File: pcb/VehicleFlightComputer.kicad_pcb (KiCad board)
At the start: 4 copper layers, 50 x 50 mm, 54 parts, among them J1 FFC2B28-24-G, J3 USB_C_Receptacle, J4 Debug, Q1 S8050, SW1 B3U-1000P, U1 STM32H533VET6, U2 LIS2MDL, U3 LSM6DSV32X, U4 MCP2221A-I/ST, U5 AP2112K-3.3

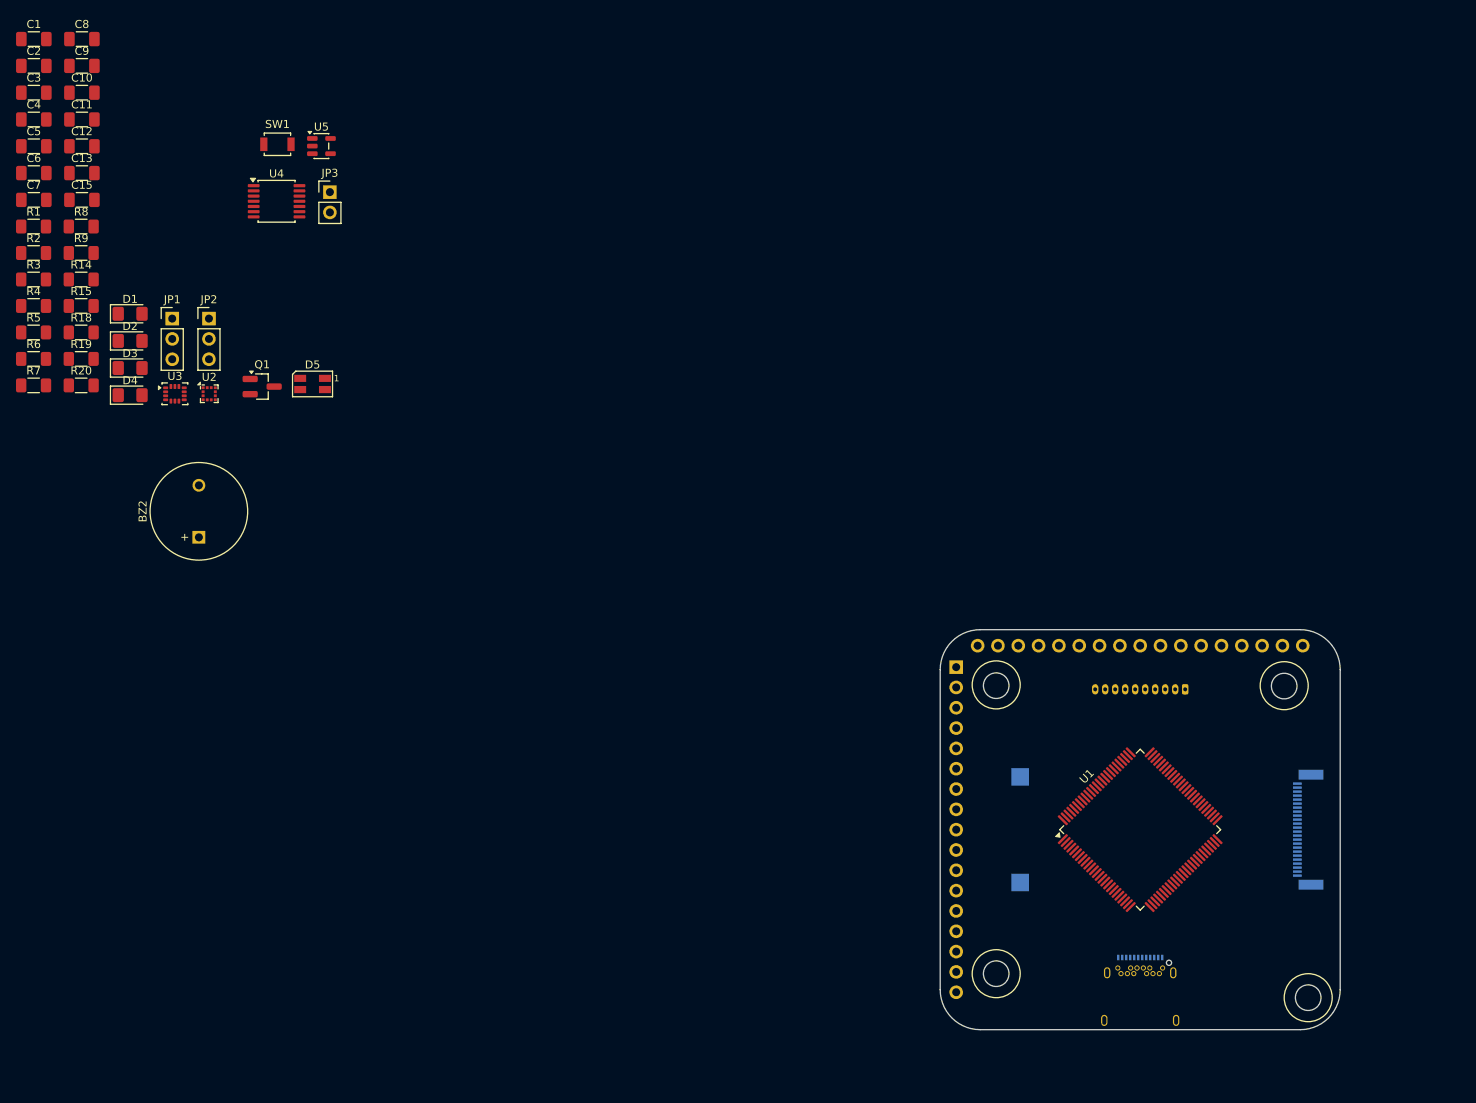
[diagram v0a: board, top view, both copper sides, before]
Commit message: Stack-up of GND-PWR/SIG-PWR/SIG-GND for shielding.
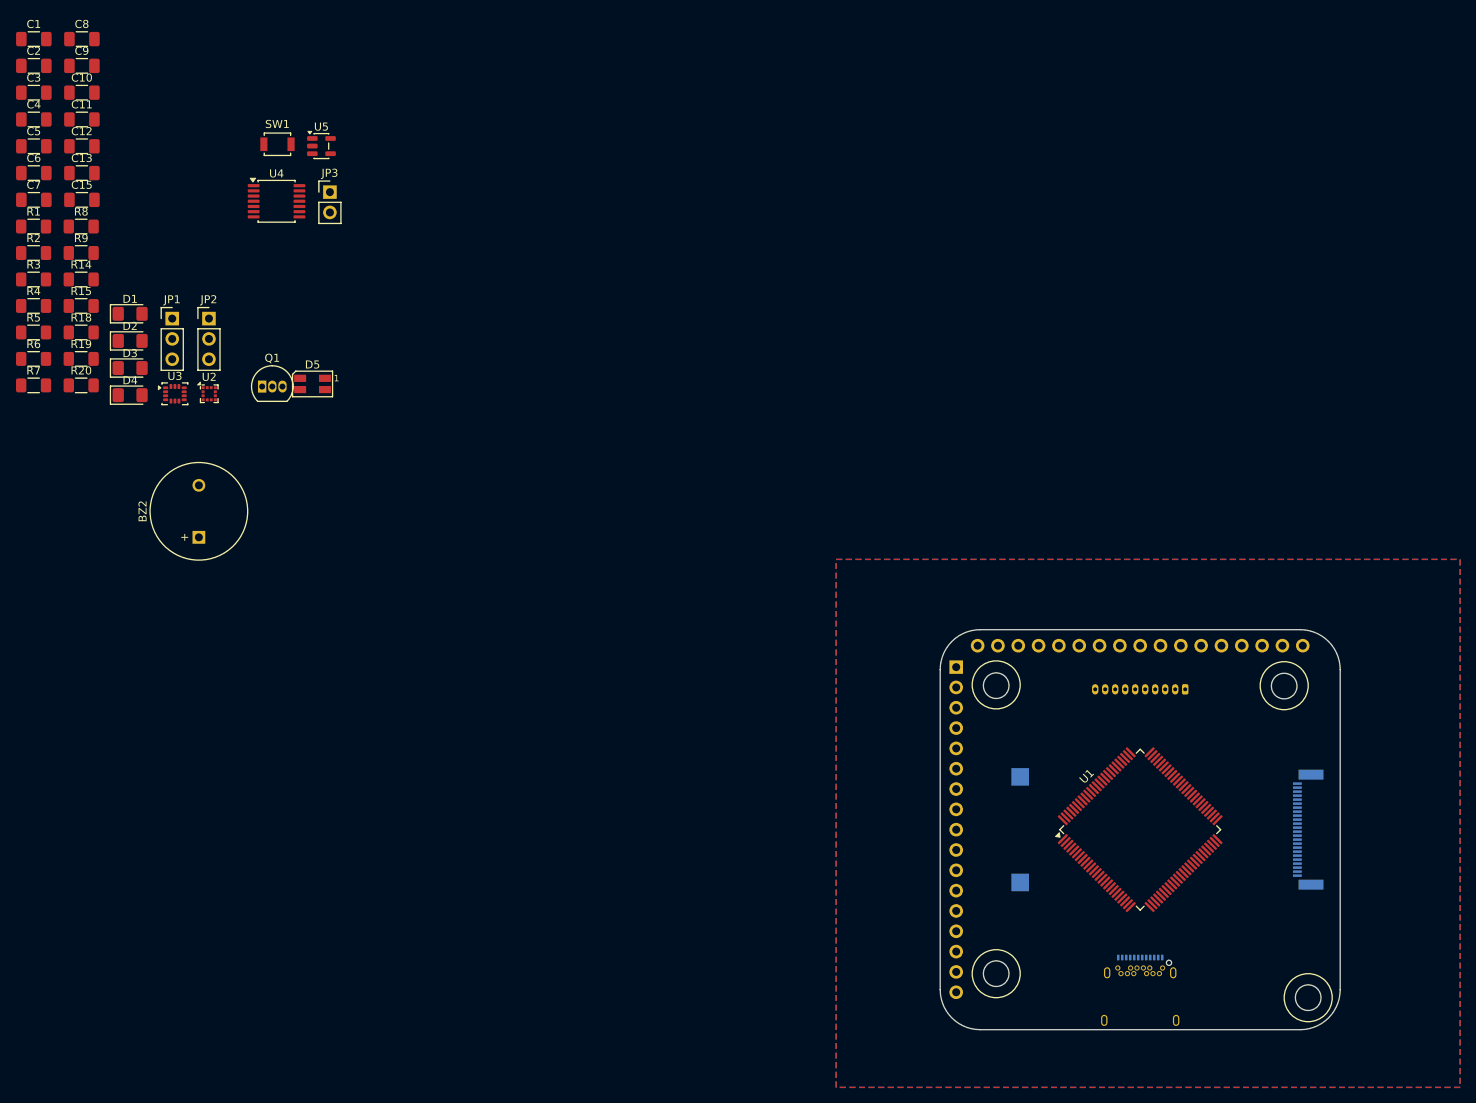
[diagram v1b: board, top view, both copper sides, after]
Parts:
- Q1: footprint Package_TO_SOT_SMD:SOT-23_Handsoldering -> Package_TO_SOT_THT:TO-92_Inline
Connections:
- J6 pad 1: unconnected-(J6-Pad1) -> +3.3V
- J6 pad 10: unconnected-(J6-Pad10) -> GND
- J6 pad 11: unconnected-(J6-Pad11) -> +3.3V
- J6 pad 12: unconnected-(J6-Pad12) -> ESP32_SPI_CLOCK
- J6 pad 13: unconnected-(J6-Pad13) -> GND
- J6 pad 14: unconnected-(J6-Pad14) -> ESP32_SPI_MOSI
- J6 pad 15: unconnected-(J6-Pad15) -> GND
- J6 pad 16: unconnected-(J6-Pad16) -> ESP32_SPI_MISO
- J6 pad 17: unconnected-(J6-Pad17) -> +3.3V
- J6 pad 18: unconnected-(J6-Pad18) -> ESP32_SPI_NSS
- J6 pad 2: unconnected-(J6-Pad2) -> OPENMV_SPI_CLOCK
- J6 pad 22: unconnected-(J6-Pad22) -> GND
- J6 pad 24: unconnected-(J6-Pad24) -> GND
- J6 pad 27: unconnected-(J6-Pad27) -> GND
- J6 pad 28: unconnected-(J6-Pad28) -> OPENMV_RESET
- J6 pad 29: unconnected-(J6-Pad29) -> ESP32_RESET
- J6 pad 3: unconnected-(J6-Pad3) -> GND
- J6 pad 4: unconnected-(J6-Pad4) -> OPENMV_SPI_MOSI
- J6 pad 5: unconnected-(J6-Pad5) -> GND
- J6 pad 6: unconnected-(J6-Pad6) -> OPENMV_SPI_MISO
- J6 pad 7: unconnected-(J6-Pad7) -> +3.3V
- J6 pad 8: unconnected-(J6-Pad8) -> OPENMV_SPI_NSS
- J6 pad 9: unconnected-(J6-Pad9) -> OPENMV_SPI_READY
- U1 pad 17: unconnected-(U1-PC2-Pad17) -> OPENMV_SPI_MISO
- U1 pad 18: unconnected-(U1-PC3-Pad18) -> OPENMV_SPI_MOSI
- U1 pad 35: unconnected-(U1-PB0-Pad35) -> ESP32_SPI_MISO
- U1 pad 36: unconnected-(U1-PB1-Pad36) -> ESP32_SPI_CLOCK
- U1 pad 42: unconnected-(U1-PE11-Pad42) -> MOTOR_STEP_X
- U1 pad 43: unconnected-(U1-PE12-Pad43) -> MOTOR_STEP_Y
- U1 pad 44: unconnected-(U1-PE13-Pad44) -> MOTOR_STEP_Z
- U1 pad 45: unconnected-(U1-PE14-Pad45) -> MOTOR_DISABLE
- U1 pad 46: unconnected-(U1-PE15-Pad46) -> MOTOR_DIR_X
- U1 pad 47: unconnected-(U1-PB10-Pad47) -> OPENMV_SPI_CLOCK
- U1 pad 51: unconnected-(U1-PB12-Pad51) -> OPENMV_SPI_NSS
- U1 pad 53: unconnected-(U1-PB14-Pad53) -> MOTOR_UART_TX
- U1 pad 54: unconnected-(U1-PB15-Pad54) -> MOTOR_UART_RX
- U1 pad 80: sd_clock -> unconnected-(U1-PC12-Pad80)
- U1 pad 82: unconnected-(U1-PD1-Pad82) -> EXTERNAL_DETECTED
- U1 pad 83: unconnected-(U1-PD2-Pad83) -> BATTERY_ALLOWED
- U1 pad 84: unconnected-(U1-PD3-Pad84) -> MOTOR_DIR_Z
- U1 pad 85: unconnected-(U1-PD4-Pad85) -> MOTOR_DIR_Y
- U1 pad 86: unconnected-(U1-PD5-Pad86) -> OPENMV_SPI_READY
- U1 pad 87: unconnected-(U1-PD6-Pad87) -> OPENMV_RESET
- U1 pad 88: unconnected-(U1-PD7-Pad88) -> ESP32_RESET
- U1 pad 91: unconnected-(U1-PB5-Pad91) -> ESP32_SPI_MOSI
- U1 pad 95: unconnected-(U1-PB8-Pad95) -> ESP32_SPI_NSS
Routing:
- added copper zone on In1.Cu, net +3.3V
- added copper zone on In2.Cu, net +3.3V
- added copper zone on B.Cu, net GND
- added copper zone on F.Cu, net GND

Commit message: Rough layout of footprints for `VehicleFlightComputer`.
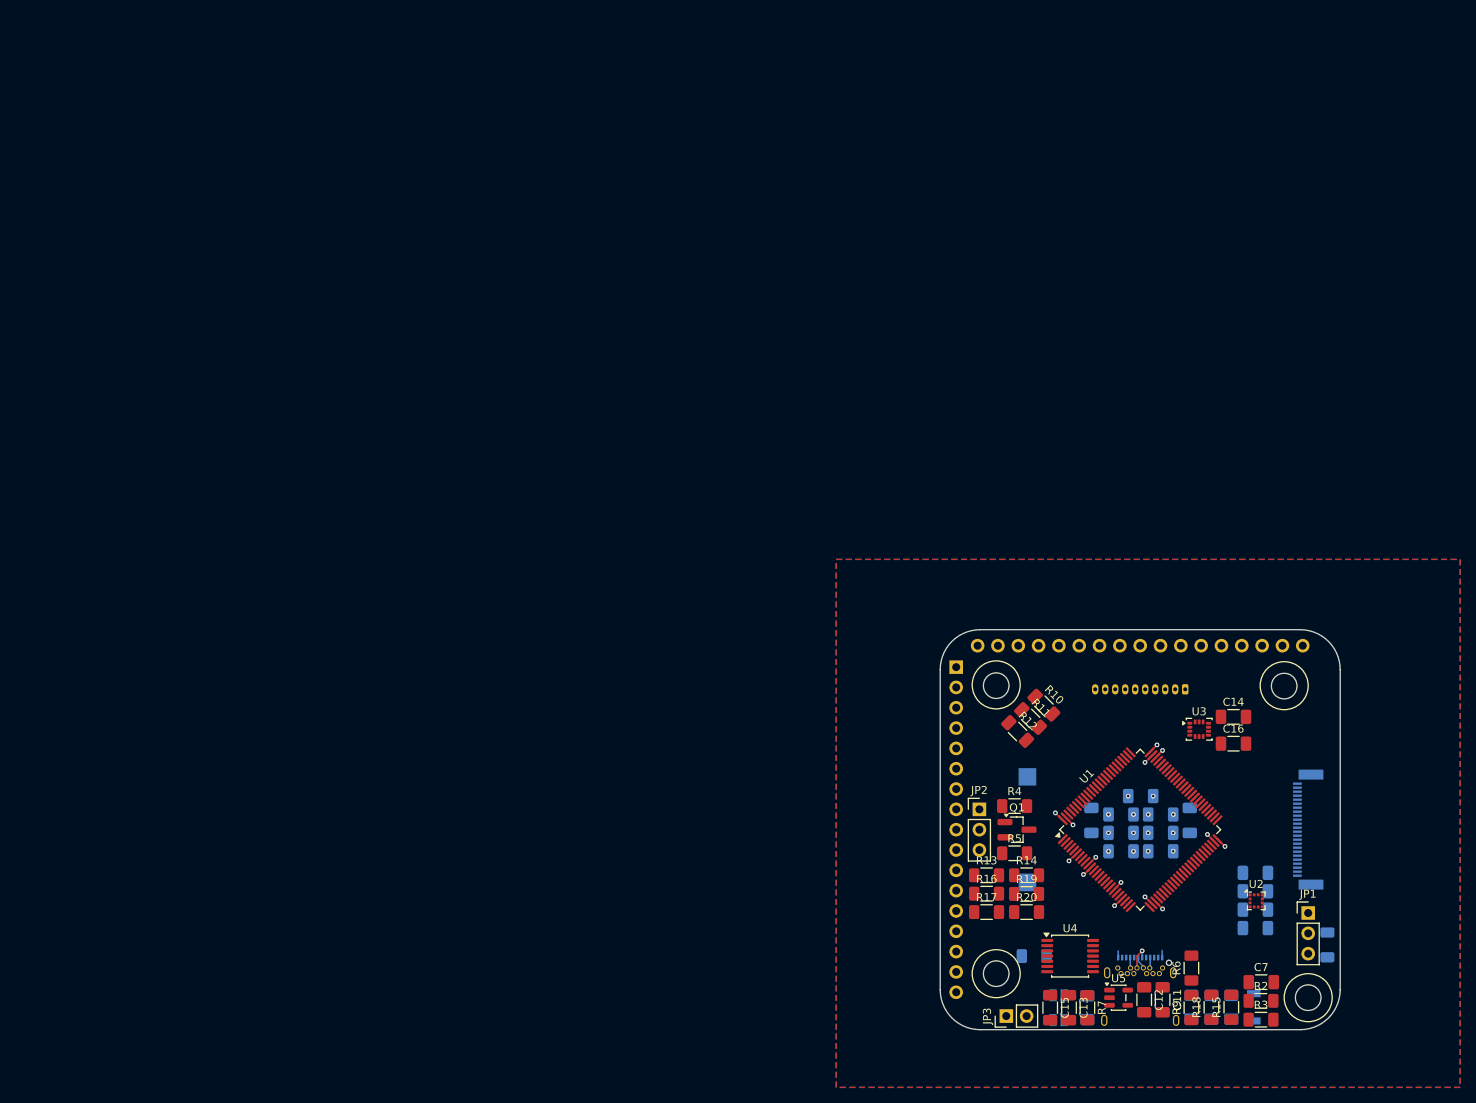
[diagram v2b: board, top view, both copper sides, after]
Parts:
- removed BZ2: WT-1205, Buzzer_Beeper:MagneticBuzzer_ProSignal_ABT-410-RC
- added C14: 100n, Capacitor_SMD:C_1206_3216Metric_Pad1.33x1.80mm_HandSolder, F.Cu at (161.7, 85.9)
- added C16: 100n, Capacitor_SMD:C_1206_3216Metric_Pad1.33x1.80mm_HandSolder, F.Cu at (161.7, 89.2)
- added C17: 220n, Capacitor_SMD:C_1206_3216Metric_Pad1.33x1.80mm_HandSolder, B.Cu at (164.4, 105.4)
- added C18: 10u, Capacitor_SMD:C_1206_3216Metric_Pad1.33x1.80mm_HandSolder, B.Cu at (164.4, 107.7)
- added C19: 100n, Capacitor_SMD:C_1206_3216Metric_Pad1.33x1.80mm_HandSolder, B.Cu at (164.4, 110.0)
- added C20: 100n, Capacitor_SMD:C_1206_3216Metric_Pad1.33x1.80mm_HandSolder, B.Cu at (164.4, 112.3)
- added R10: 47k, Resistor_SMD:R_1206_3216Metric_Pad1.30x1.75mm_HandSolder, F.Cu at (138.0, 84.4)
- added R11: 47k, Resistor_SMD:R_1206_3216Metric_Pad1.30x1.75mm_HandSolder, F.Cu at (136.3, 86.1)
- added R12: 47k, Resistor_SMD:R_1206_3216Metric_Pad1.30x1.75mm_HandSolder, F.Cu at (134.7, 87.7)
- added R13: 47k, Resistor_SMD:R_1206_3216Metric_Pad1.30x1.75mm_HandSolder, F.Cu at (130.8, 105.7)
- added R16: 47k, Resistor_SMD:R_1206_3216Metric_Pad1.30x1.75mm_HandSolder, F.Cu at (130.8, 108.0)
- added R17: 47k, Resistor_SMD:R_1206_3216Metric_Pad1.30x1.75mm_HandSolder, F.Cu at (130.8, 110.3)
- C1, C10, C2, C3, C4, C5, C6, C8, C9, D1, D2, D3, D4, D5, R1, R8, SW1: moved to B.Cu
- Q1: footprint Package_TO_SOT_THT:TO-92_Inline -> Package_TO_SOT_SMD:SOT-23_Handsoldering
- moved R1 185.0 mm to (173.4, 114.4), turned to -90 degrees
- moved C7 181.9 mm to (165.1, 119.1)
- moved R2 179.7 mm to (165.1, 121.4)
- moved R3 179.2 mm to (165.1, 123.8)
- moved C11 174.2 mm to (152.8, 121.3), turned to -90 degrees
- moved C1 171.0 mm to (152.6, 98.1)
- moved C2 170.4 mm to (152.6, 100.4)
- moved C12 170.3 mm to (150.5, 121.3), turned to -90 degrees
- moved C3 169.8 mm to (152.6, 102.7)
- moved R15 168.4 mm to (161.4, 122.2), turned to 90 degrees
- moved R9 167.8 mm to (156.4, 122.3), turned to 90 degrees
- moved C9 167.5 mm to (156.2, 98.8), turned to 90 degrees
- moved R18 164.5 mm to (158.9, 122.2), turned to 90 degrees
- moved C4 163.8 mm to (147.6, 102.7), turned to 180 degrees
- moved R6 163.5 mm to (156.4, 117.3), turned to 90 degrees
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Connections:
- U1 pad 55: unconnected-(U1-PD8-Pad55) -> OPENMV_RESET
- U1 pad 56: unconnected-(U1-PD9-Pad56) -> ESP32_RESET
- U1 pad 67: unconnected-(U1-PA8-Pad67) -> LSM6DSV32X_INTERRUPT_1
- U1 pad 68: unconnected-(U1-PA9-Pad68) -> LSM6DSV32X_INTERRUPT_2
- U1 pad 69: unconnected-(U1-PA10-Pad69) -> LSM6DSV32X_CHIP_SELECT
- U1 pad 8: unconnected-(U1-PC14-Pad8) -> LIS2MDL_DATA_READY
- U1 pad 87: OPENMV_RESET -> LIS2MDL_I2C_CLOCK
- U1 pad 88: ESP32_RESET -> LIS2MDL_I2C_DATA
- U1 pad 9: unconnected-(U1-PC15-Pad9) -> LIS2MDL_CHIP_SELECT
- U1 pad 92: unconnected-(U1-PB6-Pad92) -> LSM6DSV32X_I2C_CLOCK
- U1 pad 93: unconnected-(U1-PB7-Pad93) -> LSM6DSV32X_I2C_DATA
- U2 pad 1: unconnected-(U2-SCL/SPC-Pad1) -> LIS2MDL_I2C_CLOCK
- U2 pad 10: unconnected-(U2-Vdd_IO-Pad10) -> +3.3V
- U2 pad 3: unconnected-(U2-~{CS}-Pad3) -> LIS2MDL_CHIP_SELECT
- U2 pad 4: unconnected-(U2-SDA/SDI/SDO-Pad4) -> LIS2MDL_I2C_DATA
- U2 pad 5: unconnected-(U2-C1-Pad5) -> Net-(U2-C1)
- U2 pad 6: unconnected-(U2-GND-Pad6)_1 -> GND
- U2 pad 7: unconnected-(U2-DRDY-Pad7) -> LIS2MDL_DATA_READY
- U2 pad 8: unconnected-(U2-GND-Pad6) -> GND
- U2 pad 9: unconnected-(U2-Vdd-Pad9) -> +3.3V
- U3 pad 1: unconnected-(U3-SDO/SA0-Pad1) -> Net-(JP4-C)
- U3 pad 12: unconnected-(U3-CS-Pad12) -> LSM6DSV32X_CHIP_SELECT
- U3 pad 13: unconnected-(U3-SCL-Pad13) -> LSM6DSV32X_I2C_CLOCK
- U3 pad 14: unconnected-(U3-SDA-Pad14) -> LSM6DSV32X_I2C_DATA
- U3 pad 2: unconnected-(U3-SDx/AH1/Qvar1-Pad2) -> GND
- U3 pad 3: unconnected-(U3-SCx/AH2/Qvar2-Pad3) -> GND
- U3 pad 4: unconnected-(U3-INT1-Pad4) -> LSM6DSV32X_INTERRUPT_1
- U3 pad 5: unconnected-(U3-Vdd_IO-Pad5) -> +3.3V
- U3 pad 6: unconnected-(U3-GND-Pad6) -> GND
- U3 pad 7: unconnected-(U3-GND-Pad7) -> GND
- U3 pad 8: unconnected-(U3-Vdd-Pad8) -> +3.3V
- U3 pad 9: unconnected-(U3-INT2-Pad9) -> LSM6DSV32X_INTERRUPT_2
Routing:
- net +3.3V: track 0.00 -> 10.6 mm, vias 0 -> 15
- net GND: track 0.00 -> 9.62 mm, vias 0 -> 13
- net Net-(U4-D-): track 0.00 -> 3.24 mm, vias 0 -> 1
- net Net-(JP3-A): track 0.00 -> 2.66 mm
- net Net-(U4-D+): track 0.00 -> 1.58 mm

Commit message: `STM32 MCU Support (V1 : Smaller BOOT0 setting).`
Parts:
- removed JP1: Jumper_3_Bridged12, Connector_PinHeader_2.54mm:PinHeader_1x03_P2.54mm_Vertical
- removed R1: 10K, Resistor_SMD:R_1206_3216Metric_Pad1.30x1.75mm_HandSolder
- added R21: 47k, Resistor_SMD:R_1206_3216Metric_Pad1.30x1.75mm_HandSolder, B.Cu at (171.1, 111.7)
- added SW2: B3U-1000P, Button_Switch_SMD:SW_SPST_B3U-1000P, F.Cu at (171.1, 111.7)

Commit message: `USB-UART Bridge (V8 : Enable with solder-bridge).`
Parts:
- removed JP3: Jumper_2_Small_Bridged, Connector_PinHeader_2.54mm:PinHeader_1x02_P2.54mm_Vertical
- added JP1: SolderJumper_2_Open, Jumper:SolderJumper-2_P1.3mm_Open_RoundedPad1.0x1.5mm, F.Cu at (134.7, 123.2)

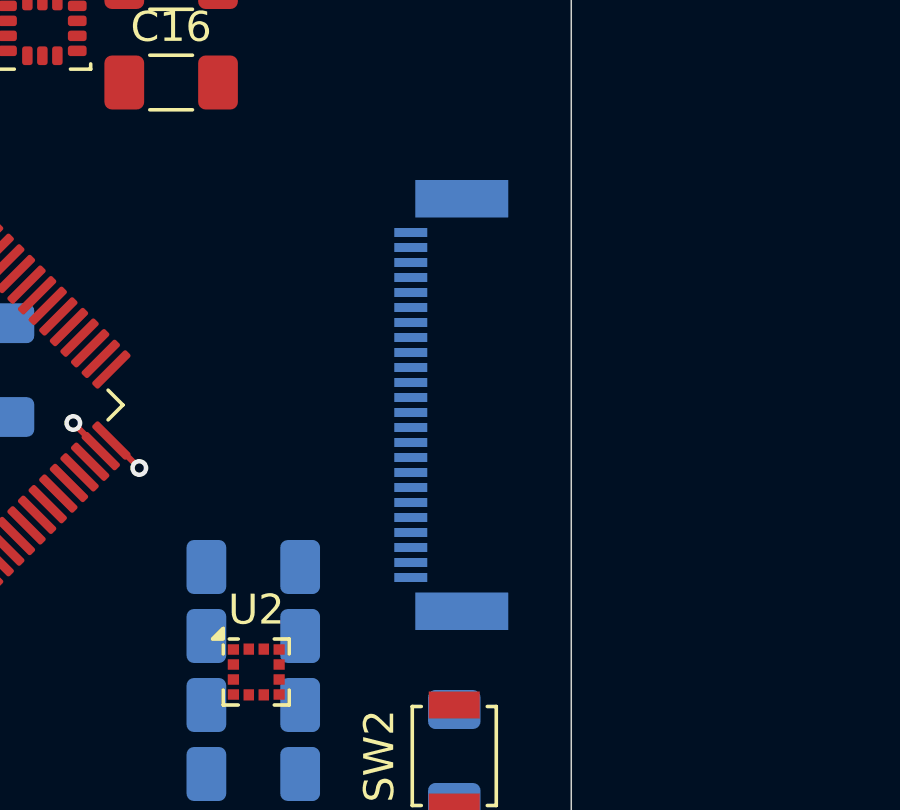
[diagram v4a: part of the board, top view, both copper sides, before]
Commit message: Repositioned the vehicle PDS I/O connector.
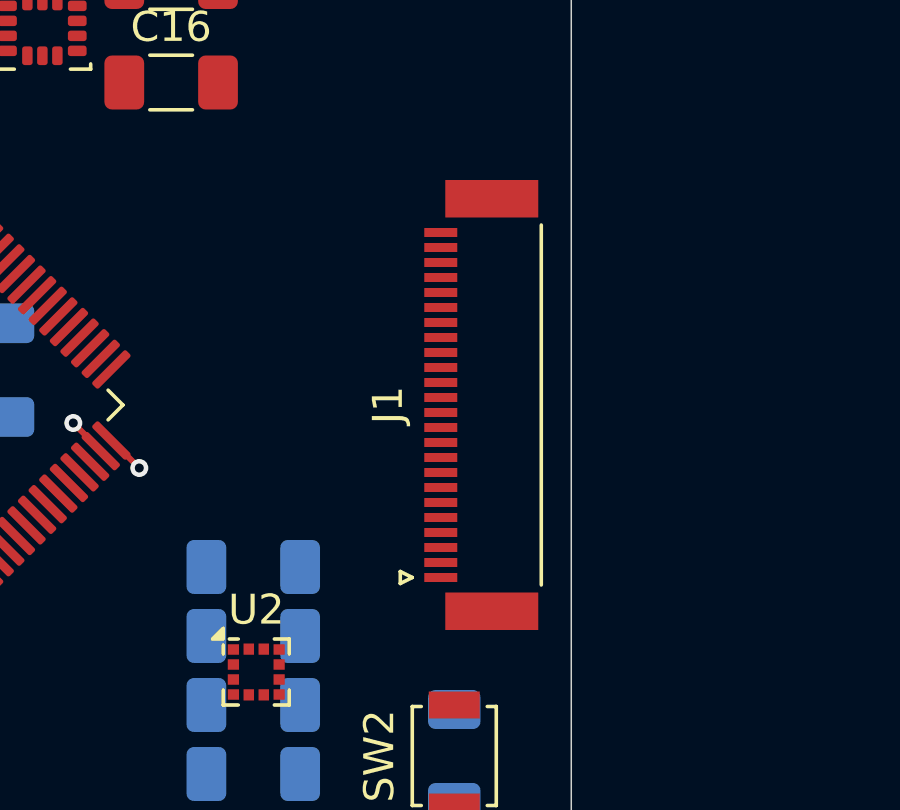
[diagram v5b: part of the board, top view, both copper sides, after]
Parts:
- J1: moved to F.Cu
- moved J1 1.00 mm to (172.0, 100.0), turned to 90 degrees
